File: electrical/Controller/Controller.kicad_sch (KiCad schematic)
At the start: 33 parts, among them J1 USB4105-GF-A, J2 SWD_10, J3 TC2030-NL, U1 LP5912-3.3DRV, U2 USBLC6-2P6, U3 STM32L072CBTx, U4 ABPMRRV001PD2A3

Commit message: PCB adjustments
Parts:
- H2: footprint MountingHole:MountingHole_3.2mm_M3_Pad -> MountingHole:MountingHole_3.2mm_M3; symbol Mechanical:MountingHole_Pad -> Mechanical:MountingHole
- J2: LCSC (none) -> C3333234; Part (none) -> Samtech FTSH-105-01-L-DH-TR
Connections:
- net GND: no longer H2.1
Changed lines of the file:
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@@
+			)
+		)
+		(property "LCSC" "C3333234"
+			(at 121.92 199.39 0)
+			(effects
+				(font
+					(size 1.27 1.27)
+				)
+				(hide yes)
+			)
+		)
+		(property "Part" "Samtech FTSH-105-01-L-DH-TR"
+			(at 121.92 199.39 0)
+			(effects
+				(font
+					(size 1.27 1.27)
+				)
+				(hide yes)
 			)
 		)
@@
 	)
 	(symbol
-		(lib_id "Mechanical:MountingHole_Pad")
+		(lib_id "Mechanical:MountingHole")
 		(at 322.58 73.66 0)
 		(unit 1)
@@
 			)
 		)
-		(property "Footprint" "MountingHole:MountingHole_3.2mm_M3_Pad"
+		(property "Footprint" "MountingHole:MountingHole_3.2mm_M3"
 			(at 322.58 73.66 0)
 			(effects
@@
 			)
 		)
-		(property "Description" "Mounting Hole with connection"
+		(property "Description" "Mounting Hole without connection"
 			(at 322.58 73.66 0)
 			(effects
@@
 				(hide yes)
 			)
-		)
-		(pin "1"
 		)
 		(instances
@@
 					(unit 1)
 				)
-			)
-		)
-	)
-	(symbol
-		(lib_id "power:GND")
-		(at 322.58 76.2 0)
-		(unit 1)
-		(exclude_from_sim no)
-		(in_bom yes)
-		(on_board yes)
-		(dnp no)
-		(fields_autoplaced yes)
-		(property "Reference" "#PWR032"
-			(at 322.58 82.55 0)
-			(effects
-				(font
-					(size 1.27 1.27)
-				)
-				(hide yes)
-			)
-		)
-		(property "Value" "GND"
-			(at 322.58 81.28 0)
-			(effects
-				(font
-					(size 1.27 1.27)
-				)
-				(hide yes)
-			)
-		)
-		(property "Footprint" ""
-			(at 322.58 76.2 0)
-			(effects
-				(font
-					(size 1.27 1.27)
-				)
-				(hide yes)
-			)
-		)
-		(property "Datasheet" ""
-			(at 322.58 76.2 0)
-			(effects
-				(font
-					(size 1.27 1.27)
-				)
-				(hide yes)
-			)
-		)
-		(property "Description" "Power symbol creates a global label with name \"GND\" , ground"
-			(at 322.58 76.2 0)
-			(effects
-				(font
-					(size 1.27 1.27)
-				)
-				(hide yes)
-			)
-		)
-		(pin "1"
-		)
-		(instances
-			(project "control"
-				(path "/da26d94e-7a50-4b99-9678-5aaaf6987a15"
-					(reference "#PWR032")
-					(unit 1)
-				)

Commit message: Add licenses
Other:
- company: Bushel Basket Musical Instruments -> (none)
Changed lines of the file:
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@@
 	(title_block
 		(title "MIDI Concertina Controller")
-		(company "Bushel Basket Musical Instruments")
+		(comment 1 "https://ohwr.org/cern_ohl_s_v2.pdf")
+		(comment 2 "Licensed under CERN-OHL-S v2 or any later version")
+		(comment 3 "Copyright 2025 Steven Schulteis")
 	)
 	(junction

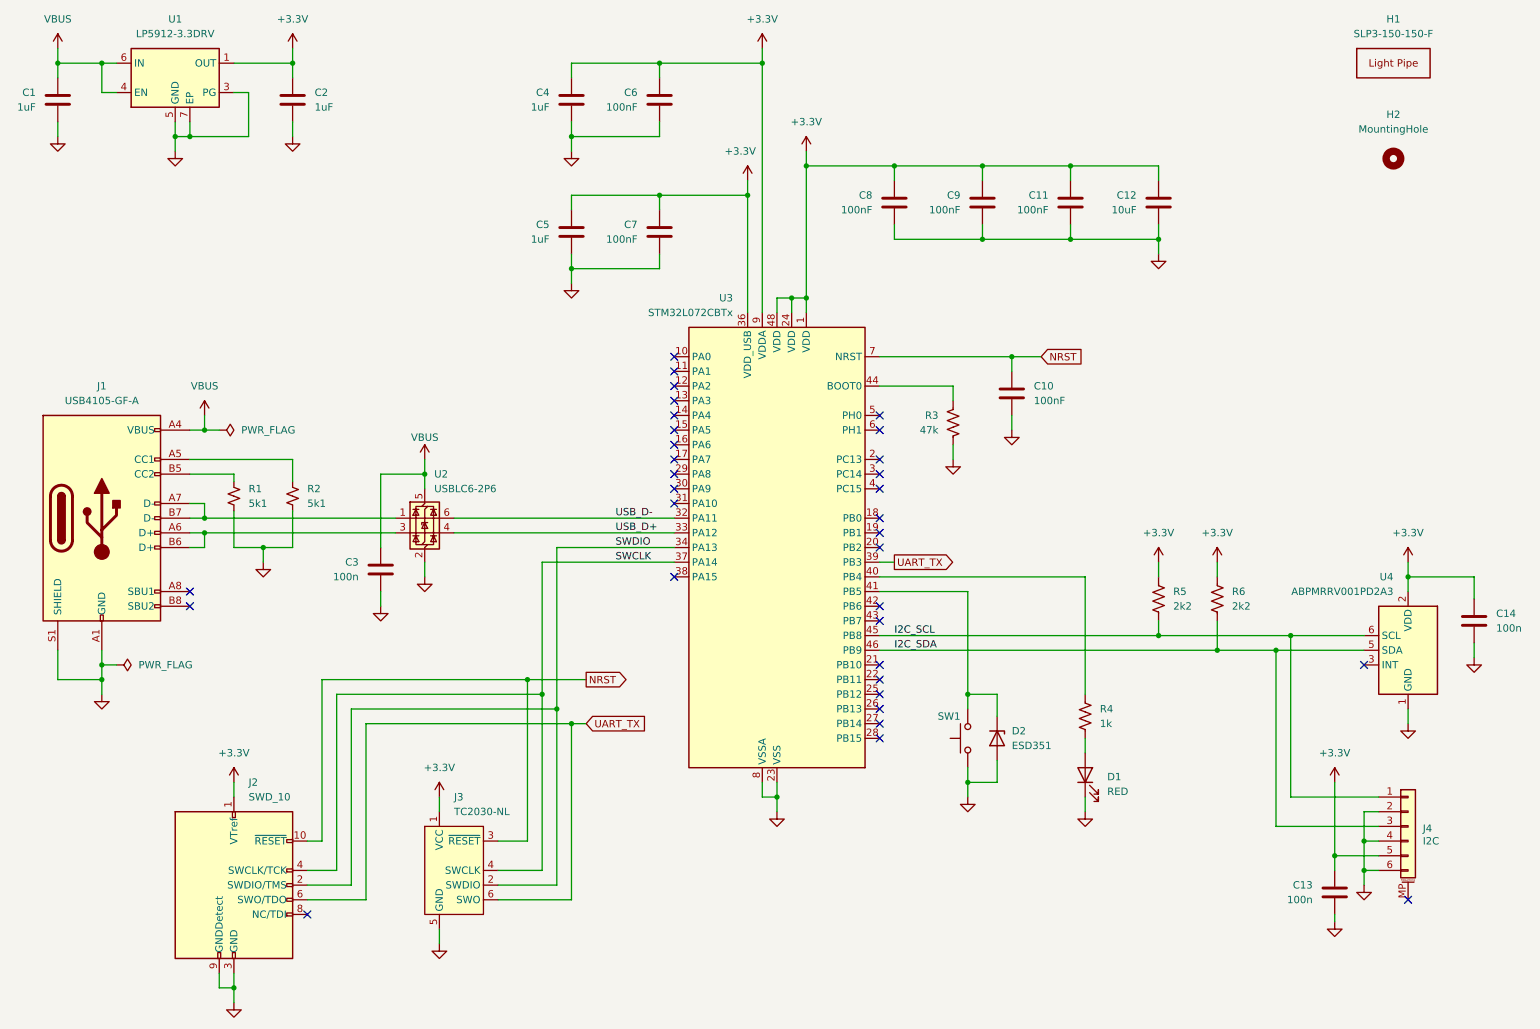
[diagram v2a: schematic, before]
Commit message: Use wide layout for controller PCB
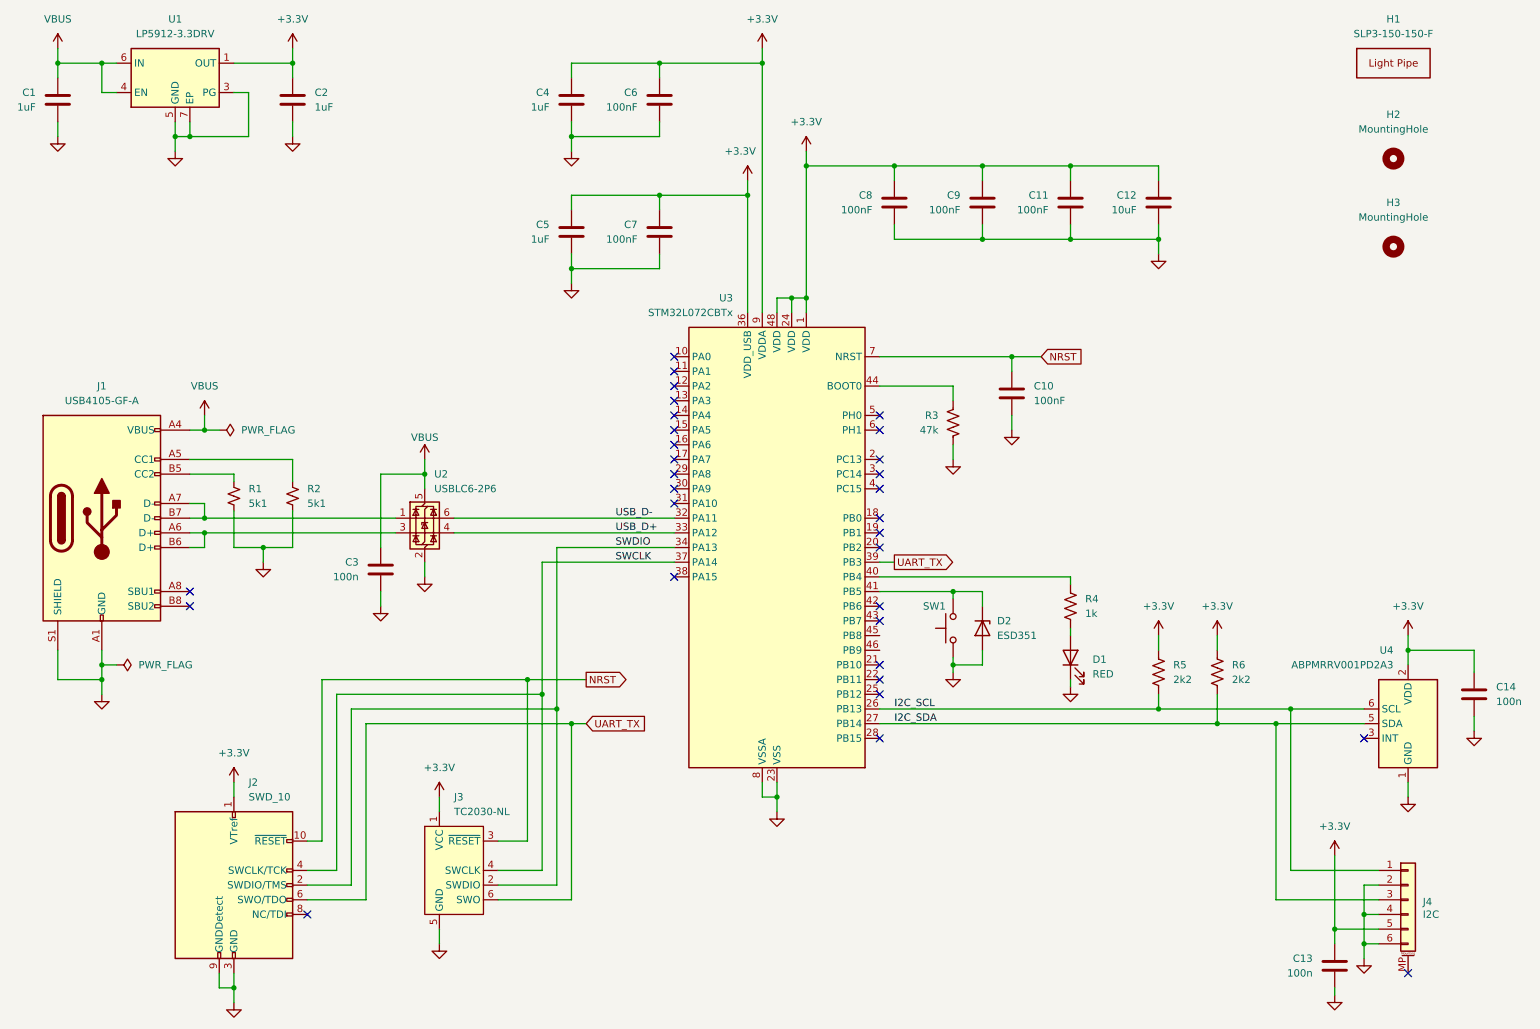
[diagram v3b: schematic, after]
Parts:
- added H3: MountingHole, MountingHole:MountingHole_3.2mm_M3, symbol Mechanical:MountingHole
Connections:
- net I2C_SCL: now also U3.26 (PB13); no longer U3.45 (PB8)
- net I2C_SDA: now also U3.27 (PB14); no longer U3.46 (PB9)
- no-connect marks 33 -> 31
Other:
- moved on the sheet: C13, C14, D1, D2, J4, R4, R5, R6, SW1, U4

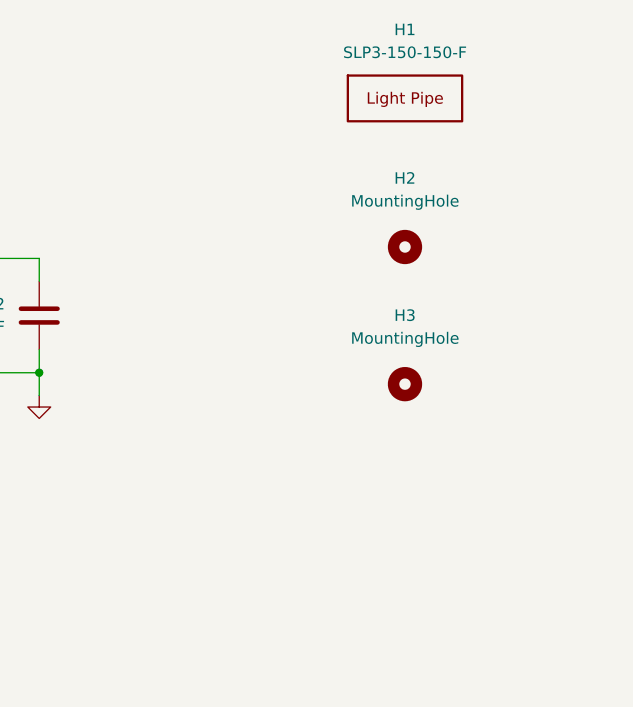
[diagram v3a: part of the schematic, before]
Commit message: Use 0402 resistors for i2c pull-ups
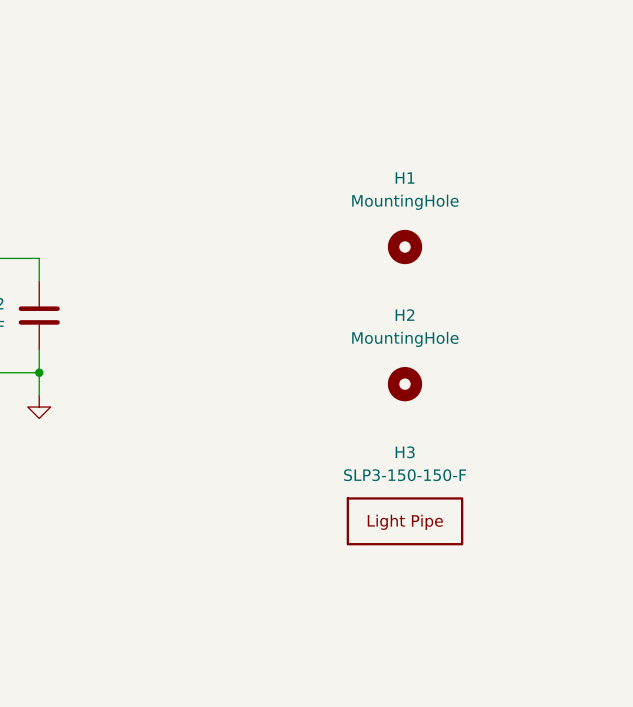
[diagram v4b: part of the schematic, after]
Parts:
- R5, R6: footprint Resistor_SMD:R_0603_1608Metric -> Resistor_SMD:R_0402_1005Metric; LCSC C4190 -> C25879; Part UNI-ROYAL 0603WAF2201T5E -> UNI-ROYAL 0402WGF2201TCE
- renumbered H2 to H1, H3 to H2, H1 to H3
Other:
- moved on the sheet: H3

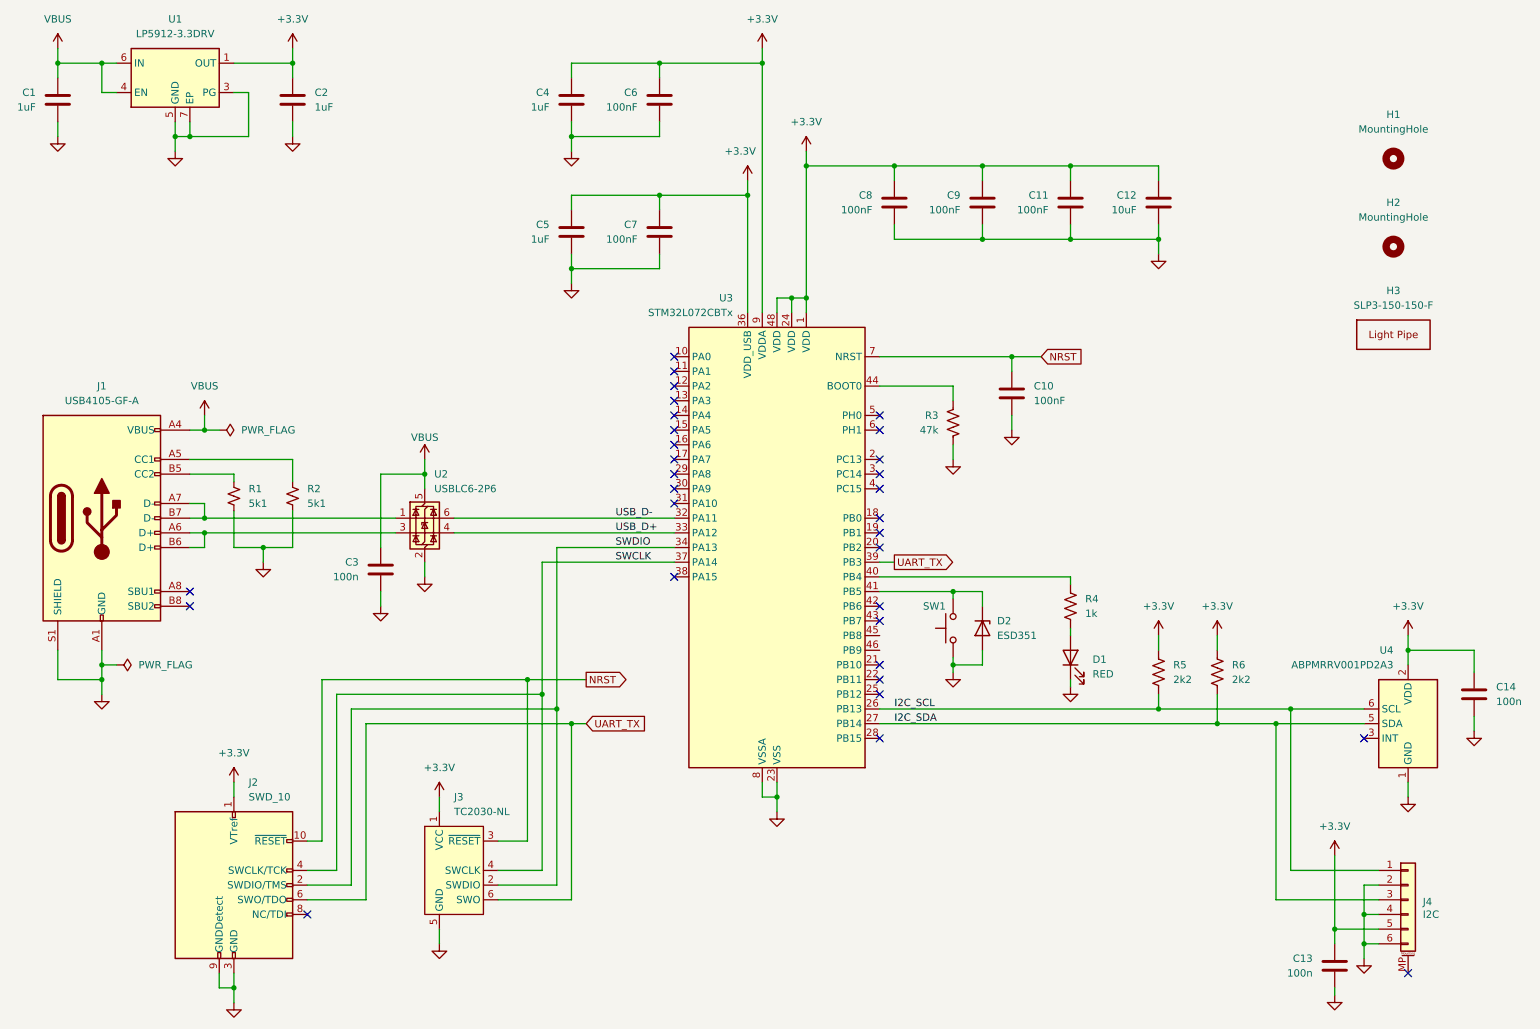
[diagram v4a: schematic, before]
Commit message: Change controller board form factor
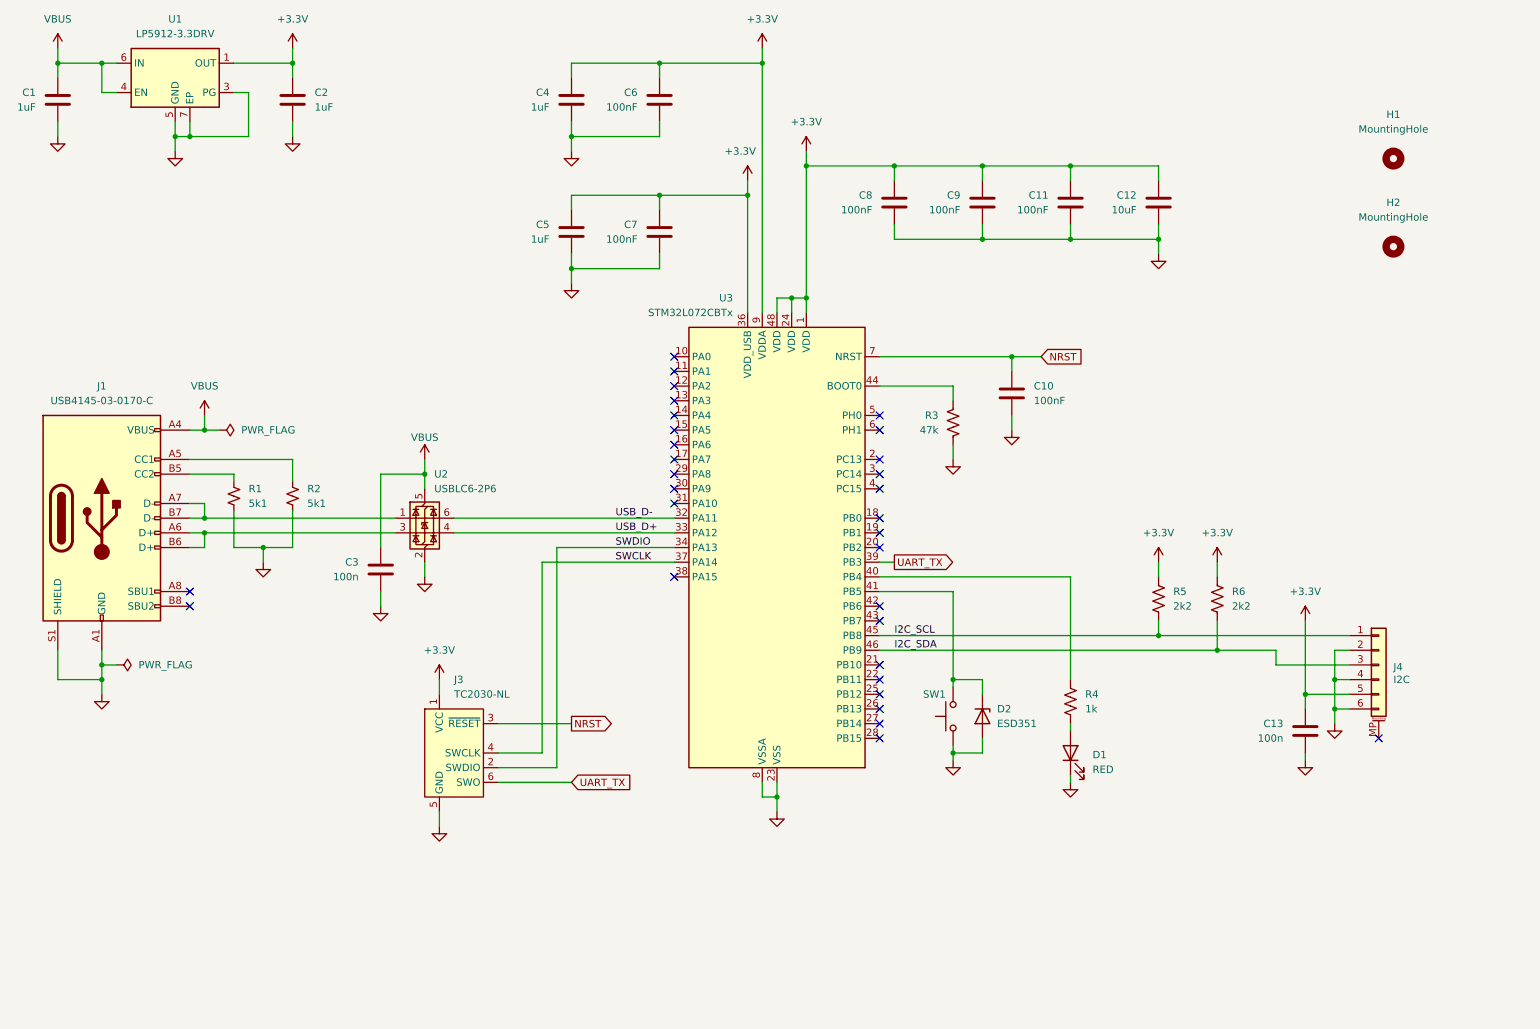
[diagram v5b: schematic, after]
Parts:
- removed C14: 100n, Capacitor_SMD:C_0402_1005Metric, symbol Device:C
- removed H3: SLP3-150-150-F, MidiConcertina:Bivar_SLP3-150-150-F, symbol MidiConcertina:LightPipe
- removed J2: SWD_10, MidiConcertina:Samtech_FTSH-105-01-L-DH, symbol Connector:Conn_ARM_JTAG_SWD_10
- removed U4: ABPMRRV001PD2A3, MidiConcertina:Honeywell_ABPMRRx, symbol MidiConcertina:Honeywell_ABPx2x
- J1: value USB4105-GF-A -> USB4145-03-0170-C; footprint Connector_USB:USB_C_Receptacle_GCT_USB4105-xx-A_16P_TopMnt_Horizontal -> MidiConcertina:USB_C_Receptacle_GCT-USB4145; LCSC C2988369 -> C5181332; Part G-Switch GT-USB-7010ASV -> GCT USB4145-03-0170-C
- R1, R2: footprint Resistor_SMD:R_0402_1005Metric -> Resistor_SMD:R_0603_1608Metric; LCSC C25905 -> C23186; Part UNI-ROYAL 0402WGF5101TCE -> UNI-ROYAL 0603WAF5101T5E
- R5, R6: footprint Resistor_SMD:R_0402_1005Metric -> Resistor_SMD:R_0603_1608Metric; LCSC C25879 -> C22939; Part UNI-ROYAL 0402WGF2201TCE -> UNI-ROYAL 0603WAF220KT5E
- SW1: footprint Button_Switch_SMD:Panasonic_EVQPUL_EVQPUC -> Button_Switch_SMD:SW_Push_1P1T_NO_E-Switch_TL3301NxxxxxG; LCSC C79175 -> C273519; Part Panasonic EVQPUL02K -> E-Switch TL3301AF160QG
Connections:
- net I2C_SCL: now also U3.45 (PB8); no longer U3.26 (PB13)
- net I2C_SDA: now also U3.46 (PB9); no longer U3.27 (PB14)
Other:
- moved on the sheet: C13, D1, D2, J3, J4, R4, R5, R6, SW1

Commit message: Minor corrections to controller design
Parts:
- C13, C3: value 100n -> 100nF
- D2: footprint Diode_SMD:D_0402_1005Metric -> Package_SON:Texas_DPY0002A_0.6x1mm_P0.65mm
- J4: LCSC C99277 -> C17393620
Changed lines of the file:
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@@
 			)
 		)
-		(property "Value" "100n"
+		(property "Value" "100nF"
 			(at 143.51 146.0499 0)
 			(effects
@@
 			)
 		)
-		(property "Value" "100n"
+		(property "Value" "100nF"
 			(at 303.53 173.9899 0)
 			(effects
@@
 			)
 		)
-		(property "LCSC" "C99277"
+		(property "LCSC" "C17393620"
 			(at 320.04 161.29 0)
 			(effects
@@
 			)
 		)
-		(property "Footprint" "Diode_SMD:D_0402_1005Metric"
+		(property "Footprint" "Package_SON:Texas_DPY0002A_0.6x1mm_P0.65mm"
 			(at 251.46 170.18 0)
 			(effects
